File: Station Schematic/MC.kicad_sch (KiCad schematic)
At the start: 3 parts, among them U8 BluePill_STM32F103C8T6

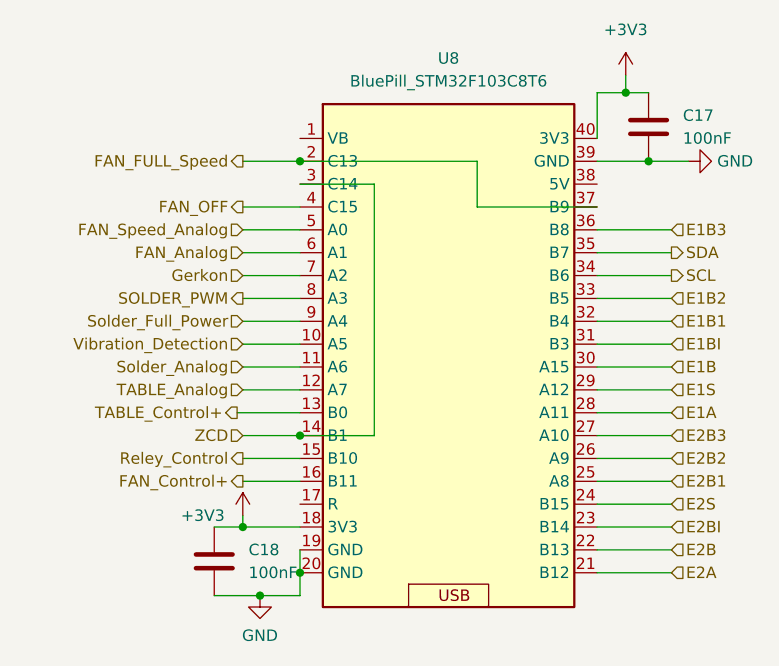
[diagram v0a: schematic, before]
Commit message: PAC was changed
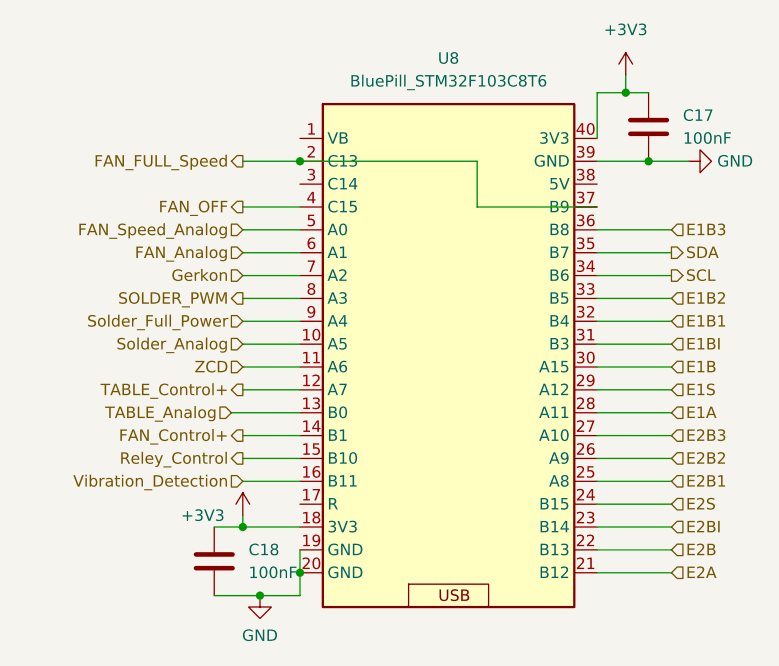
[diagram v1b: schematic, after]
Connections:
- net FAN_Control+: now also U8.14 (B1); no longer U8.16 (B11)
- net Solder_Analog: now also U8.10 (A5); no longer U8.11 (A6)
- net TABLE_Analog: now also U8.13 (B0); no longer U8.12 (A7)
- net TABLE_Control+: now also U8.12 (A7); no longer U8.13 (B0)
- net Vibration_Detection: now also U8.16 (B11); no longer U8.10 (A5)
- net ZCD: now also U8.11 (A6); no longer U8.14 (B1), U8.3 (C14)
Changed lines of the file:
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@@
-	)
-	(junction
-		(at 101.6 78.74)
-		(diameter 0)
-		(color 0 0 0 0)
 	)
 	(junction
@@
 	(wire
 		(pts
-			(xy 109.855 78.74) (xy 109.855 50.8)
-		)
-		(stroke
-			(width 0)
-			(type default)
-		)
-	)
-	(wire
-		(pts
 			(xy 101.6 96.52) (xy 101.6 93.98)
 		)
@@
 	(wire
 		(pts
-			(xy 94.615 76.2) (xy 101.6 76.2)
-		)
-		(stroke
-			(width 0)
-			(type default)
-		)
-	)
-	(wire
-		(pts
-			(xy 101.6 78.74) (xy 109.855 78.74)
+			(xy 93.98 76.2) (xy 101.6 76.2)
 		)
 		(stroke
@@
 	(wire
 		(pts
-			(xy 101.6 50.8) (xy 109.855 50.8)
-		)
-		(stroke
-			(width 0)
-			(type default)
-		)
-	)
-	(wire
-		(pts
 			(xy 95.25 66.04) (xy 101.6 66.04)
 		)
@@
 	(hierarchical_label "Vibration_Detection"
 		(shape input)
-		(at 95.25 68.58 180)
+		(at 95.25 83.82 180)
 		(fields_autoplaced yes)
 		(effects
@@
 	(hierarchical_label "Solder_Analog"
 		(shape input)
-		(at 95.25 71.12 180)
+		(at 95.25 68.58 180)
 		(fields_autoplaced yes)
 		(effects
@@
 	(hierarchical_label "ZCD"
 		(shape input)
-		(at 95.25 78.74 180)
+		(at 95.25 71.12 180)
 		(fields_autoplaced yes)
 		(effects
@@
 	(hierarchical_label "TABLE_Control+"
 		(shape output)
-		(at 94.615 76.2 180)
+		(at 95.25 73.66 180)
 		(fields_autoplaced yes)
 		(effects
@@
 	(hierarchical_label "TABLE_Analog"
 		(shape input)
-		(at 95.25 73.66 180)
+		(at 93.98 76.2 180)
 		(fields_autoplaced yes)
 		(effects
@@
 	(hierarchical_label "FAN_Control+"
 		(shape output)
-		(at 95.25 83.82 180)
-		(fields_autoplaced yes)
-		(effects
+		(at 95.25 78.74 180)
+		(fields_autoplaced yes)
+		(effects
